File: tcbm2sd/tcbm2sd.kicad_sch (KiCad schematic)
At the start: 16 parts, among them J1 TCBM, J2 JTAG, J4 AMS1117, J5 SD CARD, J8 C16-Exp-Port, U1 XC9572XL-VQ64, U2 Arduino Pro Mini

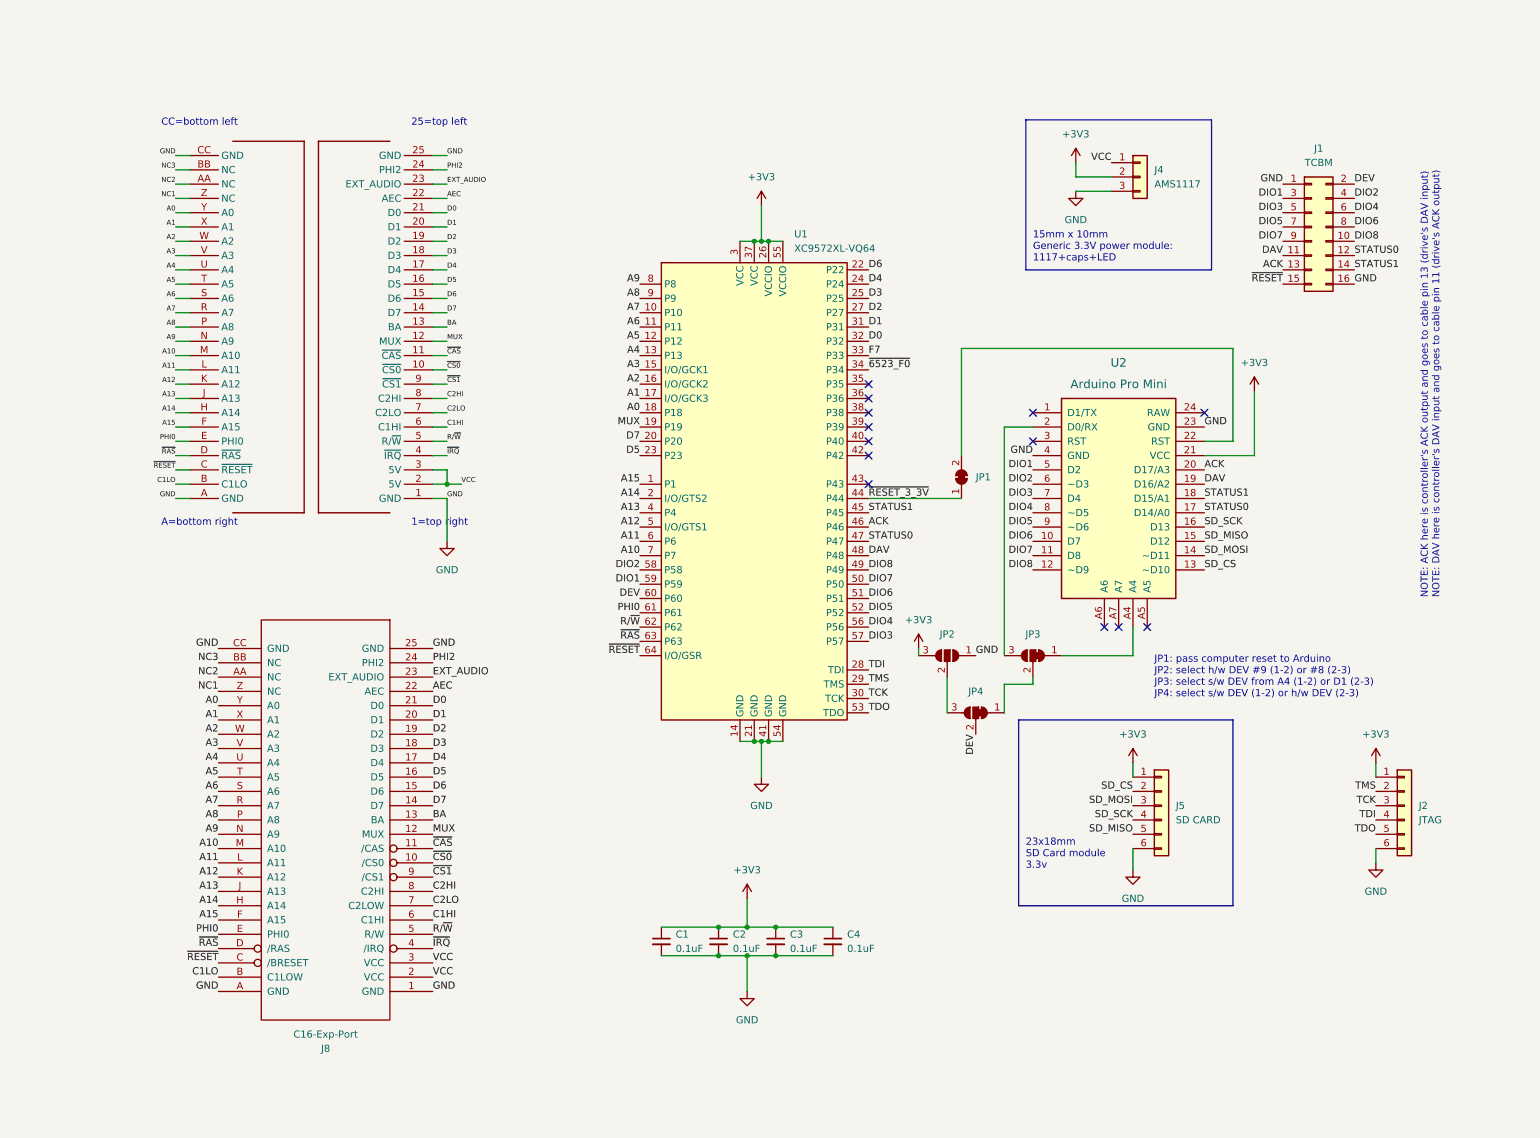
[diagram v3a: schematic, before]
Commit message: drop PLA outputs, use more exp. port inputs to CPLD (just in case) own SMD 3.3V regulator circuit own SD card circuit (SD card model etc.) from SD2IEC plug https://www.hackup.net/2018/10/sd2iecplug-v2-0/
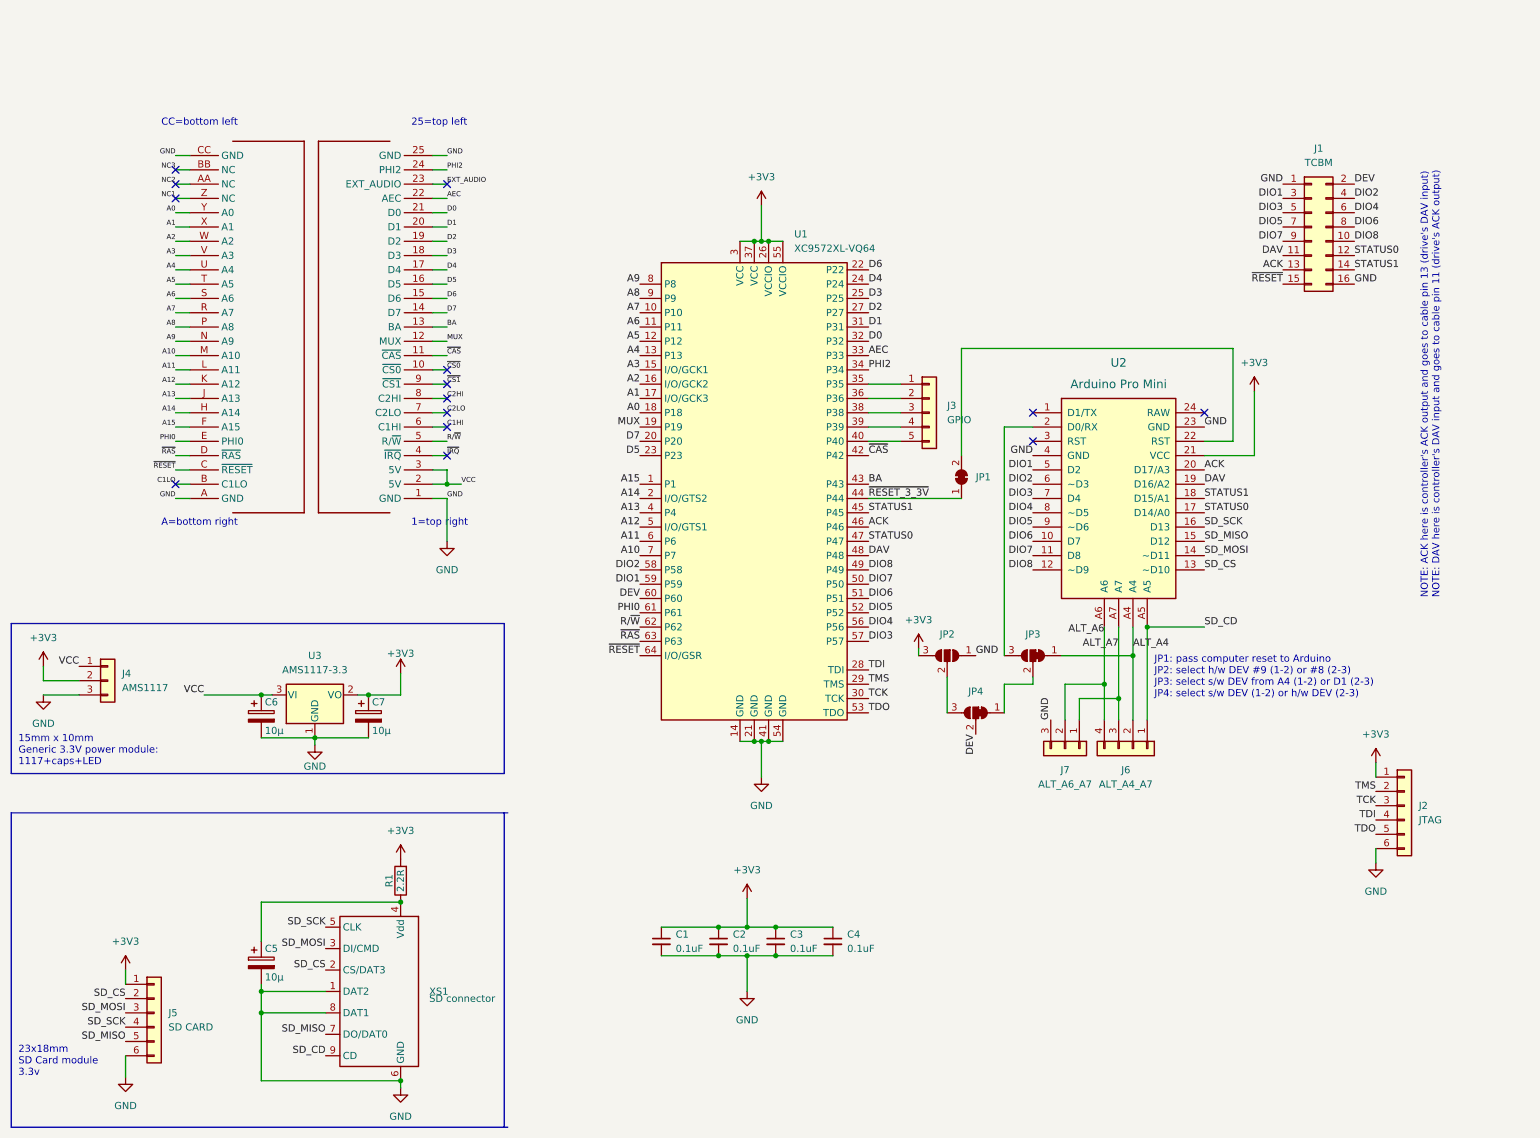
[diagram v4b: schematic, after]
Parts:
- removed J8: C16-Exp-Port, LittleSixteen:50Pin_Edge_Connector_C16, symbol Exp-Port:C16-Exp-Port
- added C5, C6, C7: 10µ, Capacitor_Tantalum_SMD:CP_EIA-3216-12_Kemet-S_Pad1.58x1.35mm_HandSolder, symbol Device:C_Polarized
- added J3: GPIO, Connector_PinHeader_2.54mm:PinHeader_1x05_P2.54mm_Vertical, symbol Connector_Generic:Conn_01x05
- added J6: ALT_A4_A7, Connector_PinHeader_2.54mm:PinHeader_1x04_P2.54mm_Vertical, symbol Connector_Generic:Conn_01x04
- added J7: ALT_A6_A7, Connector_PinHeader_2.54mm:PinHeader_1x03_P2.54mm_Vertical, symbol Connector_Generic:Conn_01x03
- added R1: 2.2R, Resistor_SMD:R_0805_2012Metric_Pad1.20x1.40mm_HandSolder, symbol Device:R
- added U3: AMS1117-3.3, Package_TO_SOT_SMD:SOT-223-3_TabPin2, symbol Regulator_Linear:AMS1117-3.3
- added XS1: SD connector, SD2IECplug:Conn_uSDcard, symbol uSD_push-push_ebay:SD_ebay-uSD-push/push_SMD
- C1, C2, C3, C4: JLCPCB Part # (none) -> C49678
- U1: JLCPCB Part # (none) -> C90569
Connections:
- net F7 is gone; now on net AEC: U1.33 (P33)
- net ~{6523_F0} is gone; now on net PHI2: U1.34 (P34)
- net +3V3: now also C7.1, R1.2, U3.2 (VO)
- net BA: now also U1.43 (P43)
- net GND: now also C5.2, C6.2, C7.2, J7.3 (Pin_3), U3.1 (GND), XS1.1 (DAT2), XS1.6 (GND), XS1.8 (DAT1)
- net SD_CS: now also XS1.2 (CS/DAT3)
- net SD_MISO: now also XS1.7 (DO/DAT0)
- net SD_MOSI: now also XS1.3 (DI/CMD)
- net SD_SCK: now also XS1.5 (CLK)
- net VCC: now also C6.1, U3.3 (VI)
- net ~{CAS}: now also U1.42 (P42)
- net ALT_A4: now reaches JP3.1 (A), U2.A4
- net ALT_A4: now also J6.2 (Pin_2)
- net SD_CD: now reaches U2.A5
- net SD_CD: now also J6.1 (Pin_1), XS1.9 (CD)
- net ALT_A6: now reaches U2.A6
- net ALT_A6: now also J6.4 (Pin_4), J7.2 (Pin_2)
- net ALT_A7: now reaches U2.A7
- net ALT_A7: now also J6.3 (Pin_3), J7.1 (Pin_1)
- net at U1.35 (P35): now also J3.1 (Pin_1)
- net at U1.36 (P36): now also J3.2 (Pin_2)
- net at U1.38 (P38): now also J3.3 (Pin_3)
- net at U1.39 (P39): now also J3.4 (Pin_4)
- net at U1.40 (P40): now also J3.5 (Pin_5)
- new net: C5.1, R1.1, XS1.4 (Vdd)
- no-connect marks 13 -> 14
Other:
- moved on the sheet: J4, J5

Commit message: add 32/64K EEPROM with /CS done using two diodes with pullup as AND one more pullup for A15 line connector for remaining Arduino lines with GND connection to short it to disable Arduino on boot
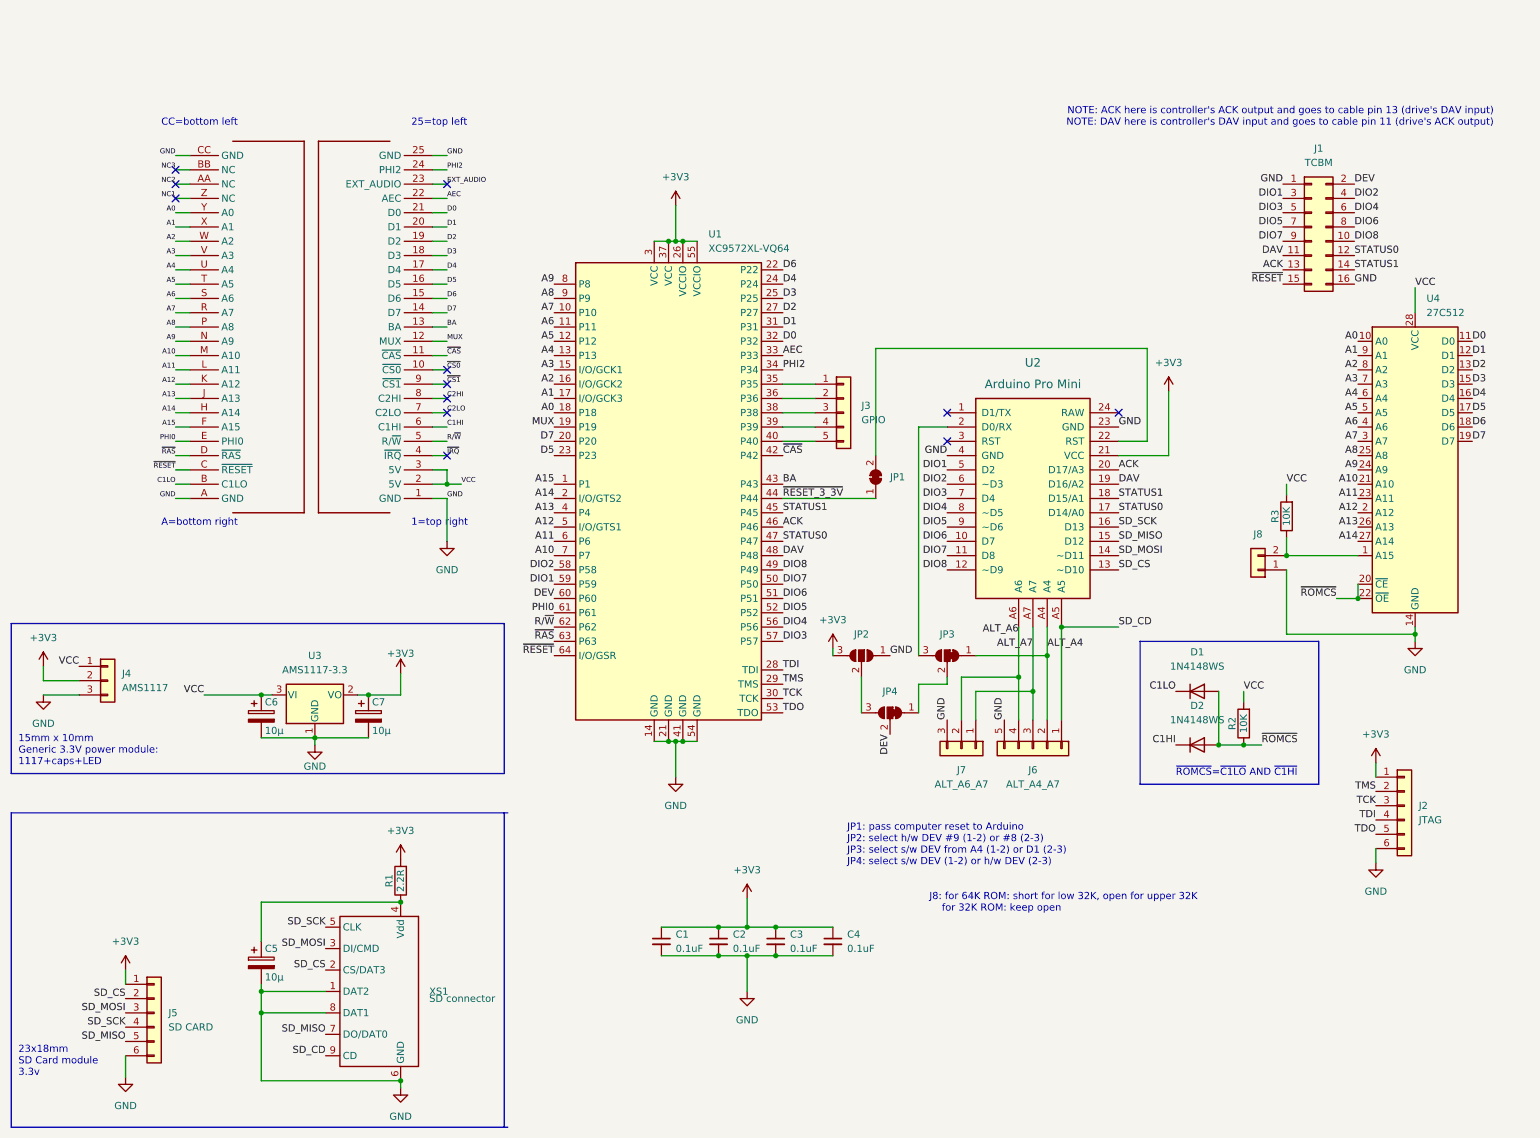
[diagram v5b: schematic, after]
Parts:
- removed J6: ALT_A4_A7, Connector_PinHeader_2.54mm:PinHeader_1x04_P2.54mm_Vertical, symbol Connector_Generic:Conn_01x04
- added D1, D2: 1N4148WS, Diode_SMD:D_SOD-323, symbol Diode:1N4148WS
- added J6: ALT_A4_A7, Connector_PinHeader_2.54mm:PinHeader_1x05_P2.54mm_Vertical, symbol Connector_Generic:Conn_01x05
- added J8: Conn_01x02, Connector_PinHeader_2.54mm:PinHeader_1x02_P2.54mm_Vertical, symbol Connector_Generic:Conn_01x02
- added R2, R3: 10K, Resistor_SMD:R_0805_2012Metric_Pad1.20x1.40mm_HandSolder, symbol Device:R
- added U4: 27C512, Package_DIP:DIP-28_W15.24mm_Socket, symbol Memory_EPROM:27C512
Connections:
- net A0: now also U4.10 (A0)
- net A1: now also U4.9 (A1)
- net A10: now also U4.21 (A10)
- net A11: now also U4.23 (A11)
- net A12: now also U4.2 (A12)
- net A13: now also U4.26 (A13)
- net A14: now also U4.27 (A14)
- net A2: now also U4.8 (A2)
- net A3: now also U4.7 (A3)
- net A4: now also U4.6 (A4)
- net A5: now also U4.5 (A5)
- net A6: now also U4.4 (A6)
- net A7: now also U4.3 (A7)
- net A8: now also U4.25 (A8)
- net A9: now also U4.24 (A9)
- net ALT_A4: now also J6.2 (Pin_2)
- net ALT_A6: now also J6.4 (Pin_4)
- net ALT_A7: now also J6.3 (Pin_3)
- net C1HI: now also D2.1 (K)
- net C1LO: now also D1.1 (K)
- net D0: now also U4.11 (D0)
- net D1: now also U4.12 (D1)
- net D2: now also U4.13 (D2)
- net D3: now also U4.15 (D3)
- net D4: now also U4.16 (D4)
- net D5: now also U4.17 (D5)
- net D6: now also U4.18 (D6)
- net D7: now also U4.19 (D7)
- net GND: now also J6.5 (Pin_5), J8.1 (Pin_1), U4.14 (GND)
- net SD_CD: now also J6.1 (Pin_1)
- net VCC: now also R2.2, R3.2, U4.28 (VCC)
- new net: J8.2 (Pin_2), R3.1, U4.1 (A15)
- new net ~{ROMCS}: D1.2 (A), D2.2 (A), R2.1, U4.20 (~{CE}), U4.22 (~{OE})
- no-connect marks 14 -> 12
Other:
- note added: "J8: for 64K ROM: short for low 32K, open for upper 32K for 32K ROM: keep open"
- note added: "~{ROMCS}=~{C1LO} AND ~{C1HI}"
- moved on the sheet: J3, J7, JP1, JP2, JP3, JP4, U1, U2

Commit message: added 32/64K EPROM and its /CS driver: 74HC00+AND gate on diodes+pullup added next/previous buttons removed A4-A7 connector (all pins occupied now) routed A6 to TCBM:16 to sense short to GND (cable attached) central hole back to 5mm
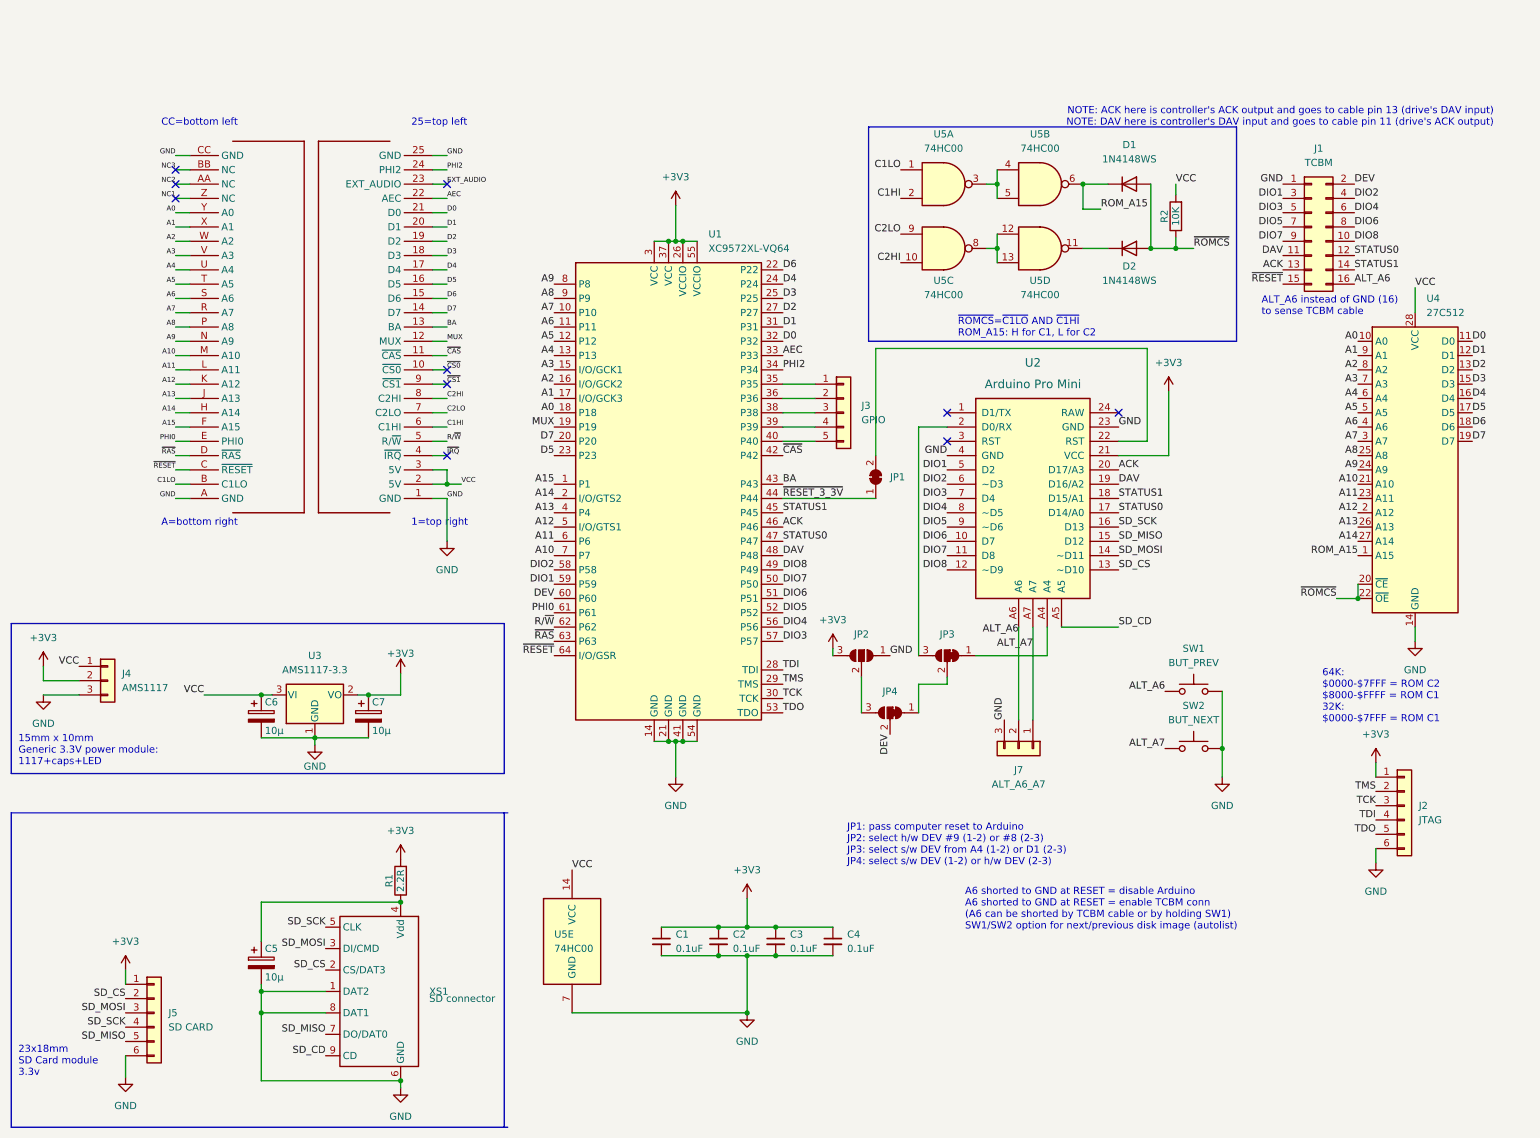
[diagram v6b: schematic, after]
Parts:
- removed J6: ALT_A4_A7, Connector_PinHeader_2.54mm:PinHeader_1x05_P2.54mm_Vertical, symbol Connector_Generic:Conn_01x05
- removed J8: Conn_01x02, Connector_PinHeader_2.54mm:PinHeader_1x02_P2.54mm_Vertical, symbol Connector_Generic:Conn_01x02
- removed R3: 10K, Resistor_SMD:R_0805_2012Metric_Pad1.20x1.40mm_HandSolder, symbol Device:R
- added SW1: BUT_PREV, Button_Switch_THT:SW_PUSH_6mm, symbol Switch:SW_Push
- added SW2: BUT_NEXT, Button_Switch_THT:SW_PUSH_6mm, symbol Switch:SW_Push
- added U5: 74HC00, Package_SO:SO-14_3.9x8.65mm_P1.27mm, symbol 74xx:74HC00
- U1: Manf (none) -> AMD/XILINX; Manf# (none) -> XC9572XL-10VQG64C
- U3: JLCPCB Part # (none) -> C6186; Manf (none) -> Advanced Monolithic Systems; Manf# (none) -> AMS1117-3.3
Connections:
- net ALT_A6: now also J1.16 (Pin_16), SW1.1
- net ALT_A7: now also SW2.1
- net C1HI: now also U5.2; no longer D2.1 (K)
- net C1LO: now also U5.1; no longer D1.1 (K)
- net C2HI: now also U5.10
- net C2LO: now also U5.9
- net GND: now also SW1.2, SW2.2, U5.7 (GND); no longer J1.16 (Pin_16)
- net VCC: now also U5.14 (VCC)
- net ROM_A15: now reaches U4.1 (A15)
- net ROM_A15: now also D1.1 (K), U5.6
- net ALT_A4: no longer names the net of JP3.1 (A), U2.A4
- new net: U5.3, U5.4, U5.5
- new net: U5.12, U5.13, U5.8
- new net: D2.1 (K), U5.11
- no-connect marks 12 -> 10
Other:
- note added: "64K: $0000-$7FFF = ROM C2 $8000-$FFFF = ROM C1 32K: $0000-$7FFF = ROM C1"
- note added: "A6 shorted to GND at RESET = disable Arduino A6 shorted to GND at RESET = enable TCBM conn (A6 can be shorted by TCBM cable or by holding SW1) SW1/SW2 option for next/previous disk image (autolist)"
- note added: "ALT_A6 instead of GND (16) to sense TCBM cable"
- note added: "~{ROMCS}=~{C1LO} AND ~{C1HI} ROM_A15: H for C1, L for C2"
- note removed: "J8: for 64K ROM: short for low 32K, open for upper 32K for 32K ROM: keep open"
- note removed: "~{ROMCS}=~{C1LO} AND ~{C1HI}"
- moved on the sheet: D1, D2, J7, R2

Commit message: production files
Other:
- note added: "~{ROMCS}=~{C1} AND ~{C2} ROM_A15: H for C1, L for C2"
- note removed: "~{ROMCS}=~{C1LO} AND ~{C1HI} ROM_A15: H for C1, L for C2"
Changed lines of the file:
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@@
   )
   (text "JP1: pass computer reset to Arduino\nJP2: select h/w DEV #9 (1-2) or #8 (2-3)\nJP3: select s/w DEV from A4 (1-2) or D1 (2-3)\nJP4: select s/w DEV (1-2) or h/w DEV (2-3)\n"
-    (at 167.64 149.225 0)
+    (at 161.29 144.145 0)
     (effects (font (size 1.27 1.27)) (justify left bottom))
   )
   (text "A6 shorted to GND at RESET = disable Arduino\nA6 shorted to GND at RESET = enable TCBM conn\n(A6 can be shorted by TCBM cable or by holding SW1)\nSW1/SW2 option for next/previous disk image (autolist)"
-    (at 188.595 160.655 0)
+    (at 196.85 154.305 0)
     (effects (font (size 1.27 1.27)) (justify left bottom))
   )
@@
     (effects (font (size 1.27 1.27)) (justify left bottom))
   )
-  (text "~{ROMCS}=~{C1LO} AND ~{C1HI}\nROM_A15: H for C1, L for C2"
+  (text "~{ROMCS}=~{C1} AND ~{C2}\nROM_A15: H for C1, L for C2"
     (at 187.325 55.245 0)
     (effects (font (size 1.27 1.27)) (justify left bottom))
